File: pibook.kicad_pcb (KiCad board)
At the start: 2 copper layers, 85 x 85 mm, 146 parts, among them IC1 ATTINY48-A, J1 ComputeModule, J2 TRS_JACK_3PIN, P1 CONN_01X40, P2 USB_OTG, P3 CONN_01X02, P4 CONN_02X05, P5 USB_A, P6 CONN_02X06, P7 CONN_01X20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

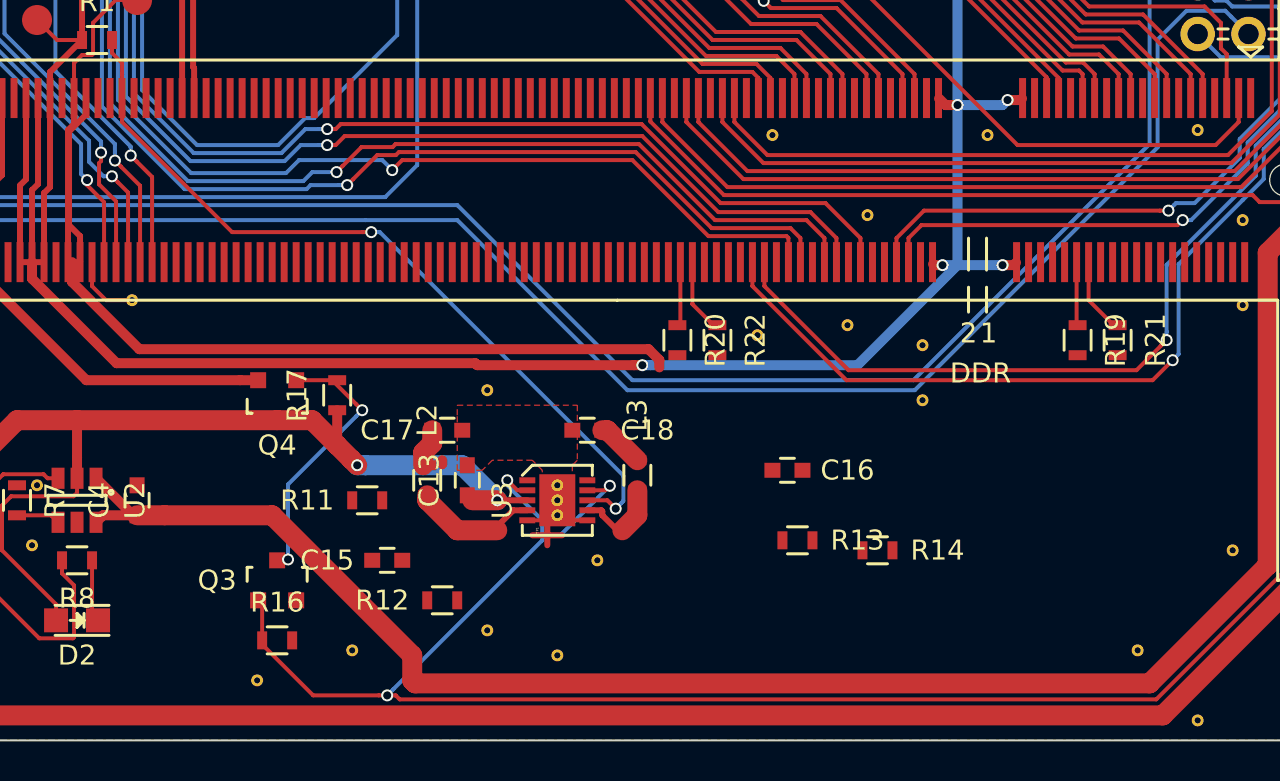
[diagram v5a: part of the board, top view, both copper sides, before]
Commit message: Routed the buck supply
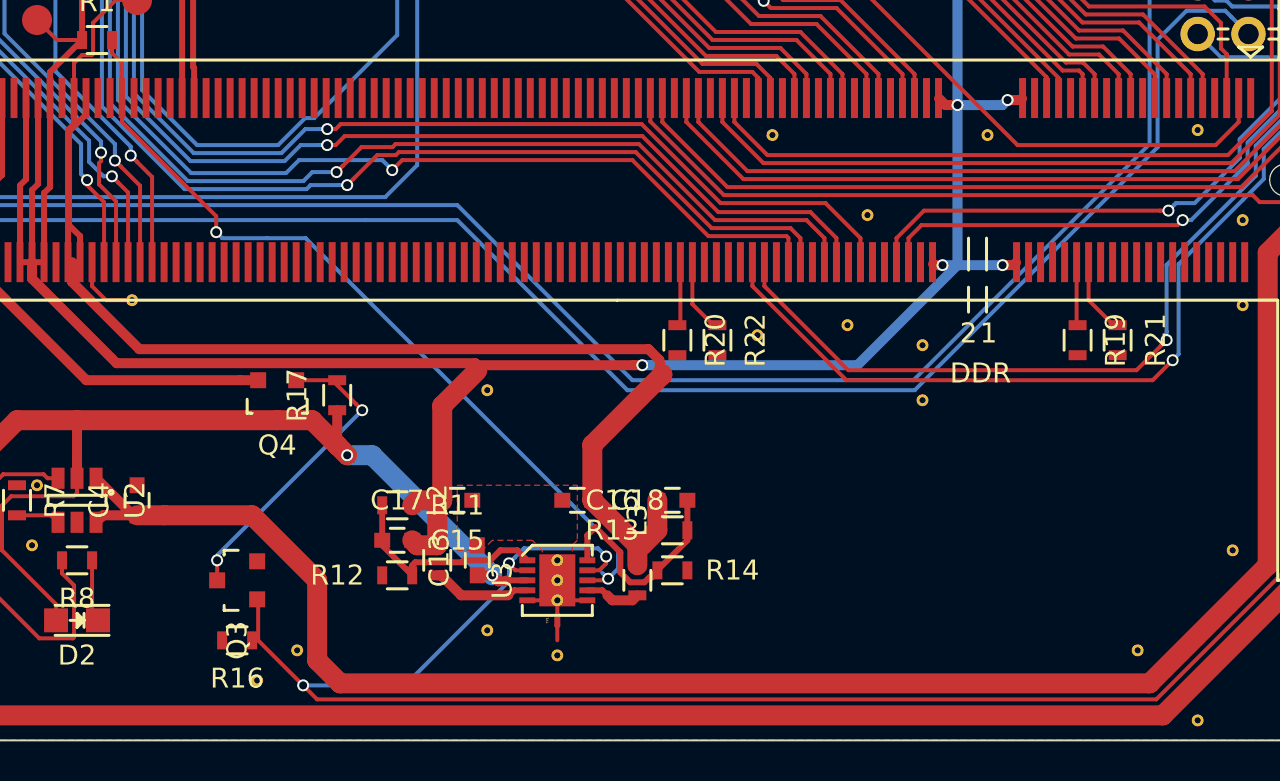
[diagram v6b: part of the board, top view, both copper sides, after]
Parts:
- removed the REF** at (117.0, 184.0)
- moved R14 10.3 mm to (120.8, 184.5)
- moved R13 6.27 mm to (120.8, 182.5), turned to 0 degrees
- moved C16 5.94 mm to (120.8, 181.0), turned to 0 degrees
- moved L3 5.25 mm to (119.0, 185.0)
- moved TP1 4.53 mm to (115.0, 187.0)
- moved REF** 4.25 mm to (115.0, 186.0)
- moved C13 4.03 mm to (111.0, 184.0)
- moved L2 4.03 mm to (109.0, 184.0)
- moved REF** 4.00 mm to (115.0, 185.0)
- moved U3 4.00 mm to (115.0, 185.0)
- moved REF** 3.75 mm to (115.0, 184.0)
- moved C17 3.54 mm to (110.0, 181.0)
- moved C18 3.54 mm to (116.0, 181.0)
- moved REF** 2.75 mm to (102.0, 188.5)
- moved R12 2.57 mm to (107.0, 184.8)
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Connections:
- J1 pad 10: (no net) -> Net-(J1-Pad10)
- J1 pad 100: (no net) -> Net-(J1-Pad100)
- J1 pad 101: (no net) -> Net-(J1-Pad101)
- J1 pad 102: (no net) -> Net-(J1-Pad102)
- J1 pad 105: (no net) -> Net-(J1-Pad105)
- J1 pad 106: (no net) -> Net-(J1-Pad106)
- J1 pad 107: (no net) -> Net-(J1-Pad107)
- J1 pad 108: (no net) -> Net-(J1-Pad108)
- J1 pad 111: (no net) -> Net-(J1-Pad111)
- J1 pad 112: (no net) -> Net-(J1-Pad112)
- J1 pad 113: (no net) -> Net-(J1-Pad113)
- J1 pad 114: (no net) -> Net-(J1-Pad114)
- J1 pad 117: (no net) -> Net-(J1-Pad117)
- J1 pad 118: (no net) -> Net-(J1-Pad118)
- J1 pad 119: (no net) -> Net-(J1-Pad119)
- J1 pad 12: (no net) -> Net-(J1-Pad12)
- J1 pad 120: (no net) -> Net-(J1-Pad120)
- J1 pad 123: (no net) -> Net-(J1-Pad123)
- J1 pad 124: (no net) -> Net-(J1-Pad124)
- J1 pad 125: (no net) -> Net-(J1-Pad125)
- J1 pad 126: (no net) -> Net-(J1-Pad126)
- J1 pad 128: (no net) -> Net-(J1-Pad128)
- J1 pad 129: (no net) -> Net-(J1-Pad129)
- J1 pad 130: (no net) -> Net-(J1-Pad130)
- J1 pad 131: (no net) -> Net-(J1-Pad131)
- J1 pad 132: (no net) -> Net-(J1-Pad132)
- J1 pad 135: (no net) -> Net-(J1-Pad135)
- J1 pad 136: (no net) -> Net-(J1-Pad136)
- J1 pad 137: (no net) -> Net-(J1-Pad137)
- J1 pad 138: (no net) -> Net-(J1-Pad138)
- J1 pad 14: (no net) -> Net-(J1-Pad14)
- J1 pad 141: (no net) -> Net-(J1-Pad141)
- J1 pad 142: (no net) -> Net-(J1-Pad142)
- J1 pad 143: (no net) -> Net-(J1-Pad143)
- J1 pad 144: (no net) -> Net-(J1-Pad144)
- J1 pad 147: (no net) -> Net-(J1-Pad147)
- J1 pad 148: (no net) -> Net-(J1-Pad148)
- J1 pad 149: (no net) -> Net-(J1-Pad149)
- J1 pad 150: (no net) -> Net-(J1-Pad150)
- J1 pad 153: (no net) -> Net-(J1-Pad153)
- J1 pad 154: (no net) -> Net-(J1-Pad154)
- J1 pad 155: (no net) -> Net-(J1-Pad155)
- J1 pad 156: (no net) -> Net-(J1-Pad156)
- J1 pad 158: (no net) -> Net-(J1-Pad158)
- J1 pad 159: (no net) -> Net-(J1-Pad159)
- J1 pad 16: (no net) -> Net-(J1-Pad16)
- J1 pad 160: (no net) -> Net-(J1-Pad160)
- J1 pad 161: (no net) -> Net-(J1-Pad161)
- J1 pad 162: (no net) -> Net-(J1-Pad162)
- J1 pad 166: (no net) -> Net-(J1-Pad166)
- J1 pad 171: (no net) -> Net-(J1-Pad171)
- J1 pad 173: (no net) -> Net-(J1-Pad173)
- J1 pad 175: (no net) -> Net-(J1-Pad175)
- J1 pad 179: (no net) -> Net-(J1-Pad179)
- J1 pad 18: (no net) -> Net-(J1-Pad18)
- J1 pad 20: (no net) -> Net-(J1-Pad20)
- J1 pad 22: (no net) -> Net-(J1-Pad22)
- J1 pad 24: (no net) -> Net-(J1-Pad24)
- J1 pad 34: (no net) -> Net-(J1-Pad34)
- J1 pad 36: (no net) -> Net-(J1-Pad36)
- J1 pad 4: (no net) -> Net-(J1-Pad4)
- J1 pad 52: (no net) -> Net-(J1-Pad52)
- J1 pad 6: (no net) -> Net-(J1-Pad6)
- J1 pad 76: (no net) -> Net-(J1-Pad76)
- J1 pad 78: (no net) -> Net-(J1-Pad78)
- J1 pad 8: (no net) -> Net-(J1-Pad8)
- J1 pad 88: (no net) -> Net-(J1-Pad88)
- J1 pad 90: (no net) -> Net-(J1-Pad90)
- J1 pad 93: (no net) -> Net-(J1-Pad93)
- J1 pad 94: (no net) -> Net-(J1-Pad94)
- J1 pad 95: (no net) -> Net-(J1-Pad95)
- J1 pad 96: (no net) -> Net-(J1-Pad96)
- J1 pad 99: (no net) -> Net-(J1-Pad99)
- P1 pad 35: (no net) -> Net-(P1-Pad35)
- P1 pad 37: (no net) -> Net-(P1-Pad37)
- P1 pad 38: (no net) -> Net-(P1-Pad38)
- P1 pad 39: (no net) -> Net-(P1-Pad39)
- P1 pad 40: (no net) -> Net-(P1-Pad40)
- P2 pad 2: (no net) -> Net-(P2-Pad2)
- P2 pad 3: (no net) -> Net-(P2-Pad3)
- P2 pad 4: (no net) -> Net-(P2-Pad4)
- R16 pad 2: GNDPWR -> GND
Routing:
- net +1V8: track 59.5 -> 72.6 mm
- net Net-(C16-Pad2): track 0.00 -> 11.1 mm
- net Net-(C15-Pad2): track 0.00 -> 10.9 mm
- net +3V3: track 218.4 -> 229.0 mm
- net Net-(Q3-Pad3): track 13.5 -> 15.4 mm
- net Net-(L3-Pad1): track 4.59 -> 2.81 mm
- net +VUSB_IN: track 160.5 -> 162.1 mm
- net /CM_RUN: track 40.1 -> 41.6 mm
- net Net-(L2-Pad1): track 6.40 -> 5.02 mm
- net GND: track 21.0 -> 19.7 mm
- net +BATT: track 304.2 -> 305.1 mm
- net GNDPWR: track 3.21 -> 3.75 mm

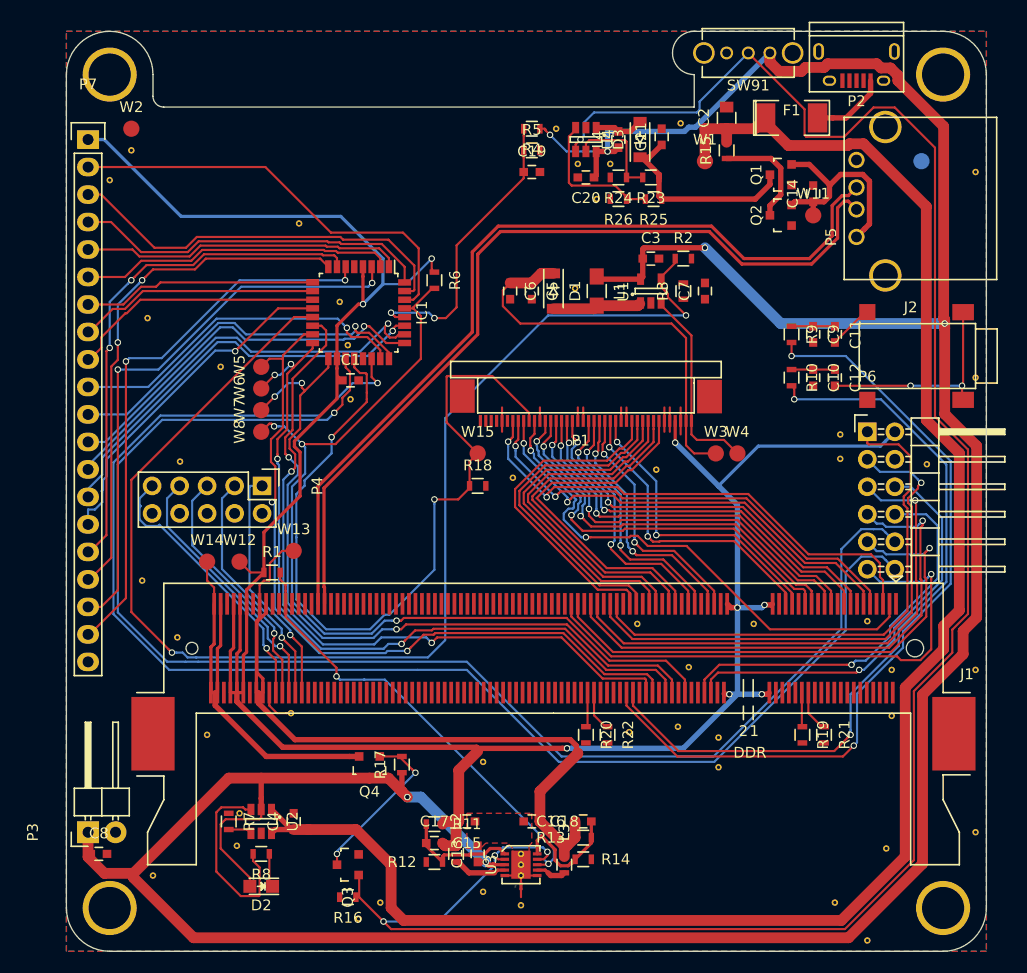
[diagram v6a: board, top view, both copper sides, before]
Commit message: Improved backlight and 5v power layout; added bleed resistor to audio filter
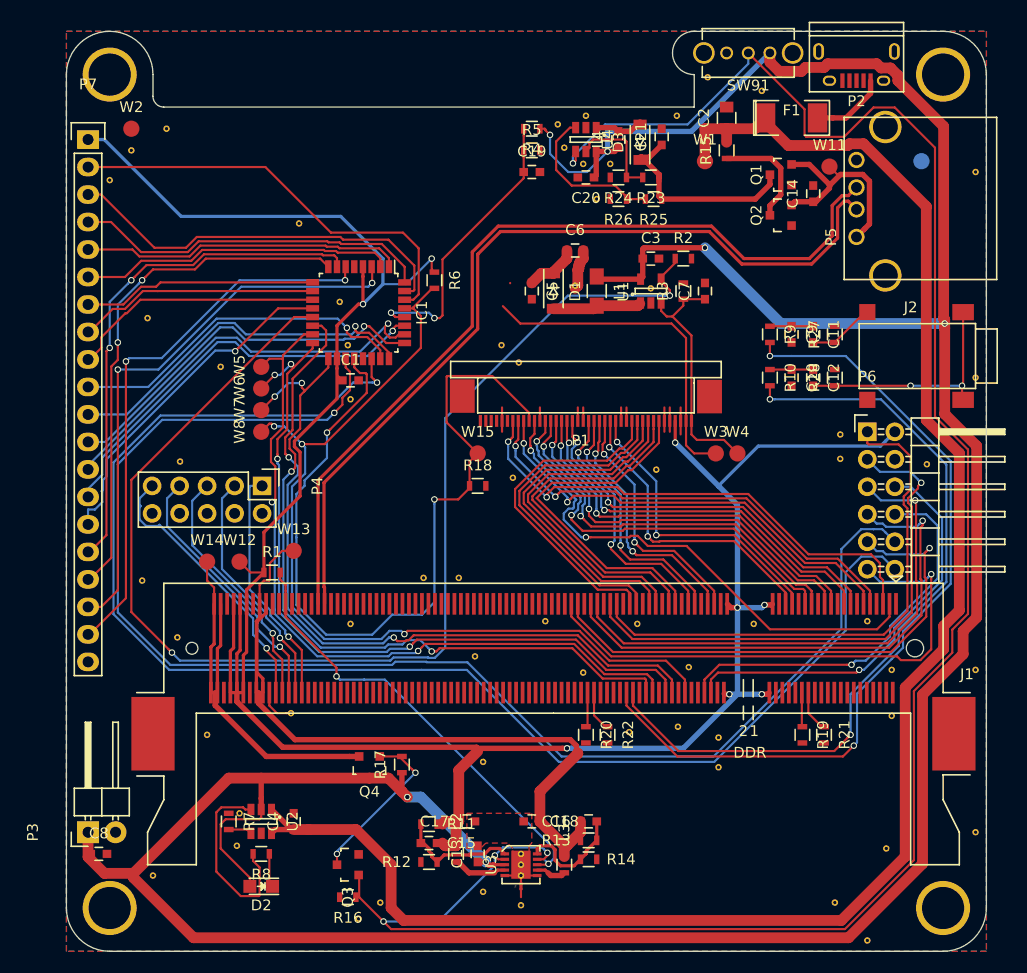
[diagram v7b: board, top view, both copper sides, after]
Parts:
- added R27: 100k, Resistors_SMD:R_0603, F.Cu at (144.0, 136.0)
- added R28: 100k, Resistors_SMD:R_0603, F.Cu at (144.0, 140.0)
- added REF**: VIA_0.6MM, ComputeModule:VIA_0.6MM, F.Cu at (113.2, 137.0)
- added REF**: VIA_0.6MM, ComputeModule:VIA_0.6MM, F.Cu at (106.0, 158.5)
- added REF**: VIA_0.6MM, ComputeModule:VIA_0.6MM, F.Cu at (99.2, 162.8)
- added REF**: VIA_0.6MM, ComputeModule:VIA_0.6MM, F.Cu at (110.8, 165.8)
- added REF**: VIA_0.6MM, ComputeModule:VIA_0.6MM, F.Cu at (120.8, 167.2)
- added REF**: VIA_0.6MM, ComputeModule:VIA_0.6MM, F.Cu at (117.2, 162.5)
- added REF**: VIA_0.6MM, ComputeModule:VIA_0.6MM, F.Cu at (114.8, 138.6)
- added REF**: VIA_0.6MM, ComputeModule:VIA_0.6MM, F.Cu at (121.0, 115.8)
- added REF**: VIA_0.6MM, ComputeModule:VIA_0.6MM, F.Cu at (119.0, 118.8)
- added REF**: VIA_0.6MM, ComputeModule:VIA_0.6MM, F.Cu at (127.0, 131.8)
- added REF**: VIA_0.6MM, ComputeModule:VIA_0.6MM, F.Cu at (82.2, 117.0)
- added REF**: VIA_0.6MM, ComputeModule:VIA_0.6MM, F.Cu at (137.2, 113.5)
- added REF**: VIA_0.6MM, ComputeModule:VIA_0.6MM, F.Cu at (132.2, 112.2)
- added REF**: VIA_0.6MM, ComputeModule:VIA_0.6MM, F.Cu at (109.2, 158.5)
- C10, C9: value 10n -> 82n
- R10, R9: value 820 -> 100
- moved C6 7.08 mm to (120.0, 128.2), turned to 0 degrees
- moved W11 4.74 mm to (143.5, 120.5)
- moved C10 2.00 mm to (140.0, 140.0)
- moved C11 2.00 mm to (142.0, 136.0)
- moved C12 2.00 mm to (142.0, 140.0)
- moved C9 2.00 mm to (140.0, 136.0)
- moved R10 2.00 mm to (138.0, 140.0)
- moved R9 2.00 mm to (138.0, 136.0)
- moved REF** 0.78 mm to (129.4, 115.8)
- moved R13 0.56 mm to (121.2, 182.8)
- moved C15 0.50 mm to (106.5, 183.0)
- moved C16 0.50 mm to (121.2, 181.0)
- moved R11 0.50 mm to (106.5, 181.2)
- moved R12 0.50 mm to (106.5, 184.8)
- moved R14 0.50 mm to (121.2, 184.5)
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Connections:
- J1 pad 10: Net-(J1-Pad10) -> (no net)
- J1 pad 100: Net-(J1-Pad100) -> (no net)
- J1 pad 101: Net-(J1-Pad101) -> (no net)
- J1 pad 102: Net-(J1-Pad102) -> (no net)
- J1 pad 105: Net-(J1-Pad105) -> (no net)
- J1 pad 106: Net-(J1-Pad106) -> (no net)
- J1 pad 107: Net-(J1-Pad107) -> (no net)
- J1 pad 108: Net-(J1-Pad108) -> (no net)
- J1 pad 111: Net-(J1-Pad111) -> (no net)
- J1 pad 112: Net-(J1-Pad112) -> (no net)
- J1 pad 113: Net-(J1-Pad113) -> (no net)
- J1 pad 114: Net-(J1-Pad114) -> (no net)
- J1 pad 117: Net-(J1-Pad117) -> (no net)
- J1 pad 118: Net-(J1-Pad118) -> (no net)
- J1 pad 119: Net-(J1-Pad119) -> (no net)
- J1 pad 12: Net-(J1-Pad12) -> (no net)
- J1 pad 120: Net-(J1-Pad120) -> (no net)
- J1 pad 123: Net-(J1-Pad123) -> (no net)
- J1 pad 124: Net-(J1-Pad124) -> (no net)
- J1 pad 125: Net-(J1-Pad125) -> (no net)
- J1 pad 126: Net-(J1-Pad126) -> (no net)
- J1 pad 128: Net-(J1-Pad128) -> (no net)
- J1 pad 129: Net-(J1-Pad129) -> (no net)
- J1 pad 130: Net-(J1-Pad130) -> (no net)
- J1 pad 131: Net-(J1-Pad131) -> (no net)
- J1 pad 132: Net-(J1-Pad132) -> (no net)
- J1 pad 135: Net-(J1-Pad135) -> (no net)
- J1 pad 136: Net-(J1-Pad136) -> (no net)
- J1 pad 137: Net-(J1-Pad137) -> (no net)
- J1 pad 138: Net-(J1-Pad138) -> (no net)
- J1 pad 14: Net-(J1-Pad14) -> (no net)
- J1 pad 141: Net-(J1-Pad141) -> (no net)
- J1 pad 142: Net-(J1-Pad142) -> (no net)
- J1 pad 143: Net-(J1-Pad143) -> (no net)
- J1 pad 144: Net-(J1-Pad144) -> (no net)
- J1 pad 147: Net-(J1-Pad147) -> (no net)
- J1 pad 148: Net-(J1-Pad148) -> (no net)
- J1 pad 149: Net-(J1-Pad149) -> (no net)
- J1 pad 150: Net-(J1-Pad150) -> (no net)
- J1 pad 153: Net-(J1-Pad153) -> (no net)
- J1 pad 154: Net-(J1-Pad154) -> (no net)
- J1 pad 155: Net-(J1-Pad155) -> (no net)
- J1 pad 156: Net-(J1-Pad156) -> (no net)
- J1 pad 158: Net-(J1-Pad158) -> (no net)
- J1 pad 159: Net-(J1-Pad159) -> (no net)
- J1 pad 16: Net-(J1-Pad16) -> (no net)
- J1 pad 160: Net-(J1-Pad160) -> (no net)
- J1 pad 161: Net-(J1-Pad161) -> (no net)
- J1 pad 162: Net-(J1-Pad162) -> (no net)
- J1 pad 166: Net-(J1-Pad166) -> (no net)
- J1 pad 171: Net-(J1-Pad171) -> (no net)
- J1 pad 173: Net-(J1-Pad173) -> (no net)
- J1 pad 175: Net-(J1-Pad175) -> (no net)
- J1 pad 179: Net-(J1-Pad179) -> (no net)
- J1 pad 18: Net-(J1-Pad18) -> (no net)
- J1 pad 20: Net-(J1-Pad20) -> (no net)
- J1 pad 22: Net-(J1-Pad22) -> (no net)
- J1 pad 24: Net-(J1-Pad24) -> (no net)
- J1 pad 34: Net-(J1-Pad34) -> (no net)
- J1 pad 36: Net-(J1-Pad36) -> (no net)
- J1 pad 4: Net-(J1-Pad4) -> (no net)
- J1 pad 52: Net-(J1-Pad52) -> (no net)
- J1 pad 6: Net-(J1-Pad6) -> (no net)
- J1 pad 76: Net-(J1-Pad76) -> (no net)
- J1 pad 78: Net-(J1-Pad78) -> (no net)
- J1 pad 8: Net-(J1-Pad8) -> (no net)
- J1 pad 88: Net-(J1-Pad88) -> (no net)
- J1 pad 90: Net-(J1-Pad90) -> (no net)
- J1 pad 93: Net-(J1-Pad93) -> (no net)
- J1 pad 94: Net-(J1-Pad94) -> (no net)
- J1 pad 95: Net-(J1-Pad95) -> (no net)
- J1 pad 96: Net-(J1-Pad96) -> (no net)
- J1 pad 99: Net-(J1-Pad99) -> (no net)
- P1 pad 35: Net-(P1-Pad35) -> (no net)
- P1 pad 37: Net-(P1-Pad37) -> (no net)
- P1 pad 38: Net-(P1-Pad38) -> (no net)
- P1 pad 39: Net-(P1-Pad39) -> (no net)
- P1 pad 40: Net-(P1-Pad40) -> (no net)
- P2 pad 2: Net-(P2-Pad2) -> (no net)
- P2 pad 3: Net-(P2-Pad3) -> (no net)
- P2 pad 4: Net-(P2-Pad4) -> (no net)
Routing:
- net /BACKL_K: track 18.3 -> 22.6 mm
- net GND: track 19.7 -> 23.6 mm
- net +BATT: track 305.1 -> 307.7 mm
- net /BACKL_PWM: track 120.0 -> 117.5 mm
- net /LCD_DISP_ON: track 73.7 -> 76.1 mm
- net /AUDIO_L_PWM: track 70.2 -> 72.3 mm
- net Net-(C12-Pad2): track 19.9 -> 21.9 mm
- net Net-(C11-Pad2): track 4.17 -> 6.17 mm
- net /AUDIO_R_PWM: track 74.5 -> 76.5 mm
- net /BACKL_A: track 37.9 -> 36.1 mm
- net Net-(R25-Pad2): track 13.2 -> 14.4 mm
- net /PWR_ENABLE: track 193.3 -> 194.5 mm
- net +1V8: track 72.6 -> 73.6 mm
- net /AVR_~RST: track 84.5 -> 83.9 mm
